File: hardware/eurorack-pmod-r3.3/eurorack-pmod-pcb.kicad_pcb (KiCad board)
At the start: 4 copper layers, 31.7 x 110 mm, 126 parts, among them J1 CONN 2x5 P=2.54mm, J10 AUDIO JACK PJ-324M0, J11 AUDIO JACK PJ-324M0, J2 CONN 2x6 P=2.54mm, J3 Conn_01x14_Socket, J4 AUDIO JACK PJ-324M0, J5 AUDIO JACK PJ-324M0, J6 AUDIO JACK PJ-324M0, J7 AUDIO JACK PJ-324M0, J8 AUDIO JACK PJ-324M0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

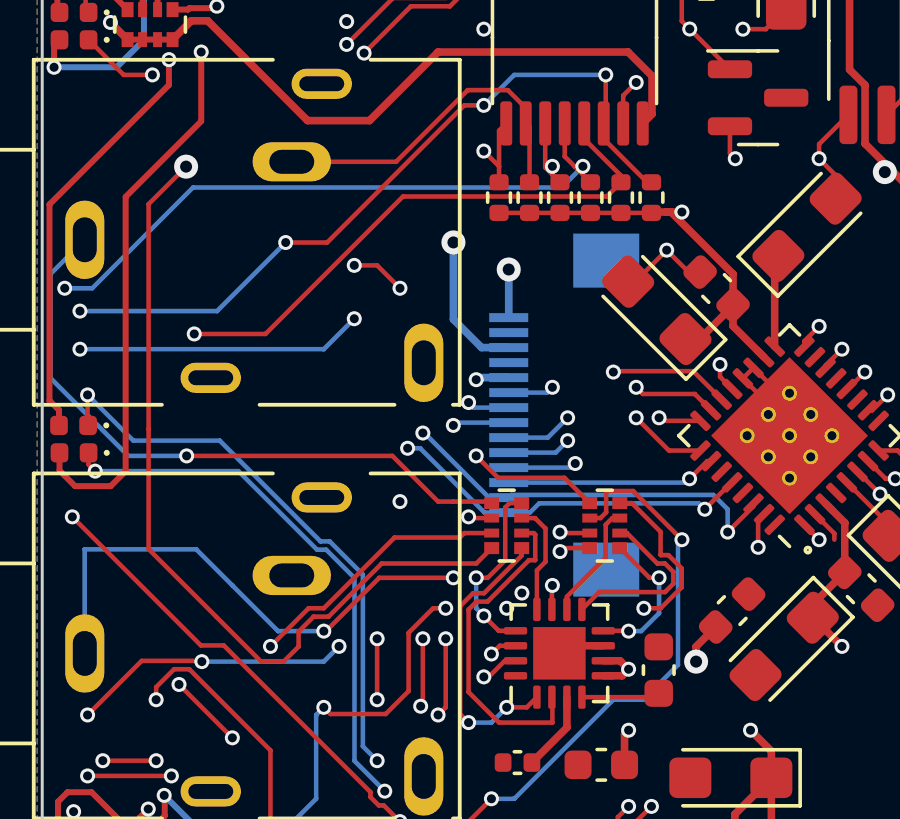
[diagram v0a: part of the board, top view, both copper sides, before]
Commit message: hardware/fab: push latest from 25.11.23 batch (#55)
* Swap FFC for CTXJ-H2.0. Pinswap capsense OUT1-4 reverse
* Convert BOM/CPL
* Add gerbers sent 25 Nov
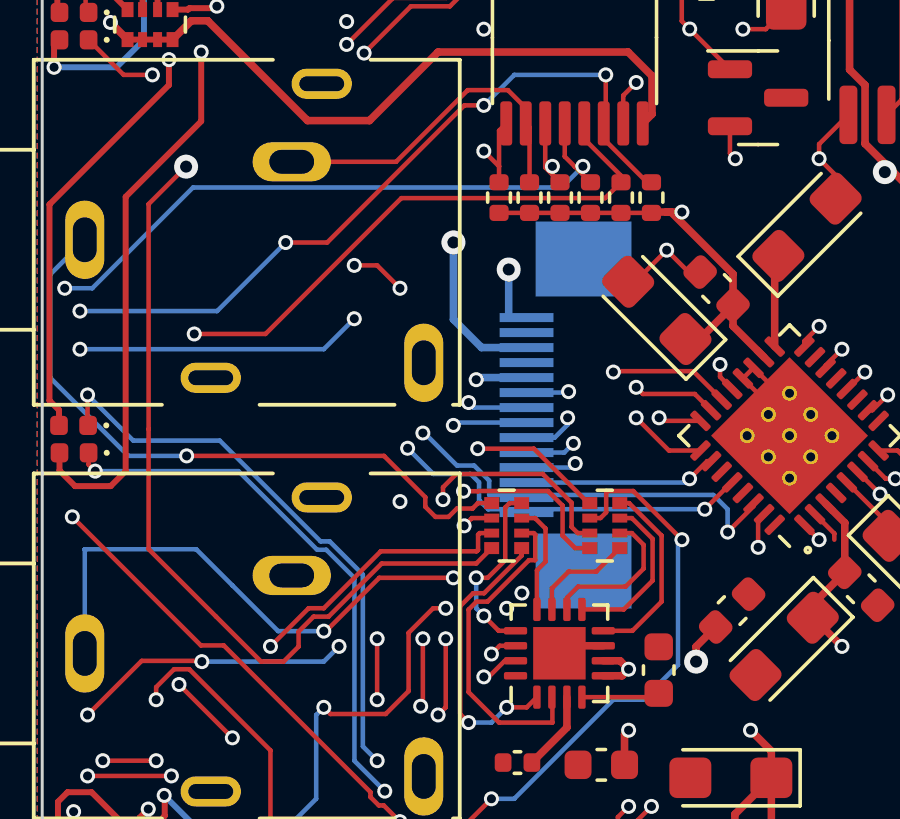
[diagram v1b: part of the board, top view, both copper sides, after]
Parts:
- J3: footprint Connector_FFC-FPC:Hirose_FH12-14S-0.5SH_1x14-1MP_P0.50mm_Horizontal -> ffc-ctxj:FFC_0.5-14P_CTXJ-H2.0_1
- moved J3 0.60 mm to (-1.80, 53.2)
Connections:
- U6 pad 10: Net-(RN13C-R3.1) -> Net-(RN13B-R2.1)
- U6 pad 11: Net-(RN13D-R4.1) -> Net-(RN13A-R1.1)
- U6 pad 8: Net-(RN13A-R1.1) -> Net-(RN13D-R4.1)
- U6 pad 9: Net-(RN13B-R2.1) -> Net-(RN13C-R3.1)
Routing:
- net /CAP_SENSE_OUT1: track 23.0 -> 26.4 mm
- net Net-(RN13D-R4.1): track 9.77 -> 6.39 mm, vias 2 -> 0
- net /CAP_SENSE_OUT2: track 31.0 -> 34.4 mm
- net Net-(RN13C-R3.1): track 3.92 -> 5.53 mm
- net Net-(RN13A-R1.1): track 5.01 -> 3.52 mm, vias 2 -> 0
- net Net-(RN13B-R2.1): track 6.12 -> 5.09 mm
- net /CAP_SENSE_IN3: track 40.4 -> 41.0 mm
- net /BICK: track 74.5 -> 75.1 mm
- net /SCL: track 111.3 -> 111.9 mm
- net /SDA: track 121.6 -> 122.2 mm
- net /CAP_SENSE_IN4: track 21.5 -> 22.1 mm

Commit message: s/apfaudio/g
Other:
- board text added: "github.com/apfaudio/eurorack-pmod"
- board text removed: "github.com/apfelaudio/eurorack-pmod"
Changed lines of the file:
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@@
     (effects (font (size 1.2 1.2) (thickness 0.25)))
   )
-  (gr_text "github.com/apfelaudio/eurorack-pmod" (at 8.086 76.758 90) (layer "B.Mask")
+  (gr_text "github.com/apfaudio/eurorack-pmod" (at 8.086 76.758 90) (layer "B.Mask")
     (effects (font (size 0.7 0.6) (thickness 0.15) italic) (justify mirror))
   )
